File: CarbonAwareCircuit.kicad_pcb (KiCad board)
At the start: 2 copper layers, 64 x 55.5 mm, 15 parts, among them J1 USB_C_Receptacle_USB2.0_14P, J2 USB_A, Q1 AO3401A, SW1 SW_Push, SW2 SW_Push, U1 LD1117V, U2 ESP32-C3-WROOM-02

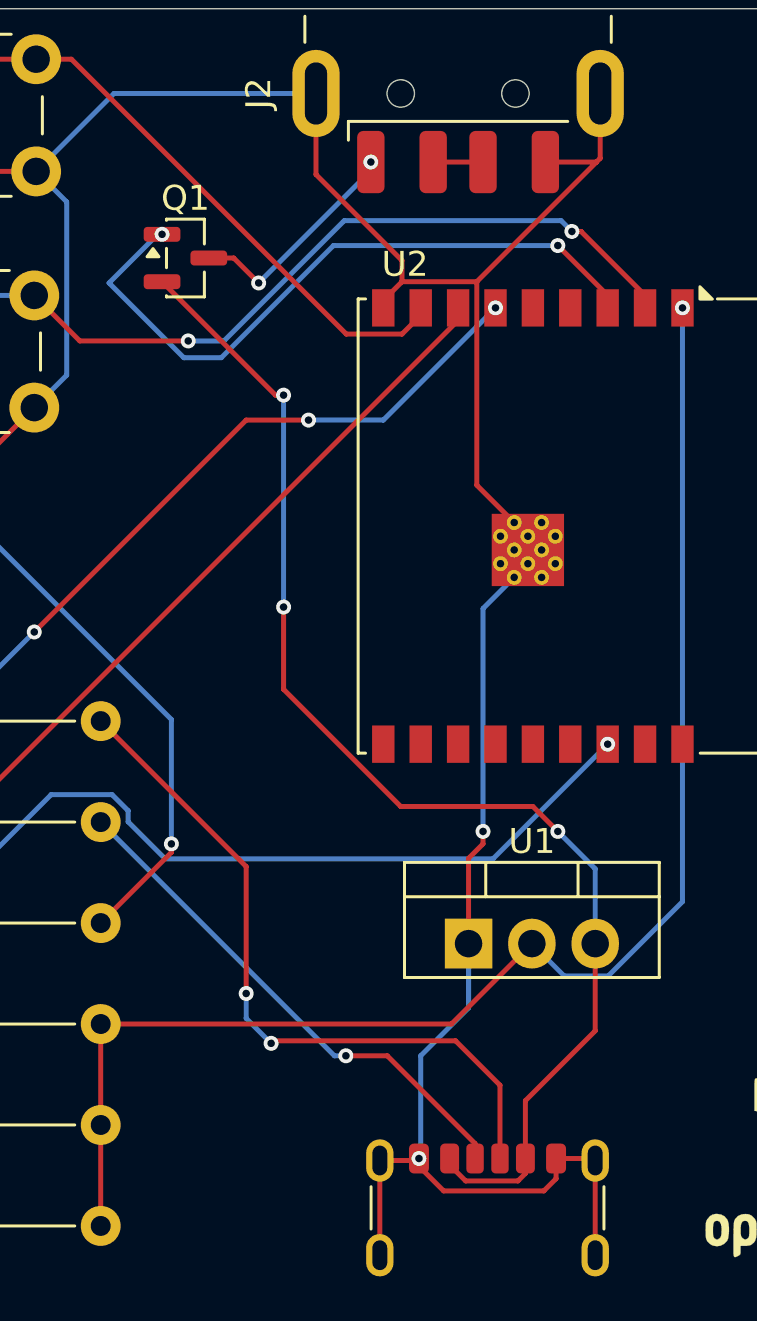
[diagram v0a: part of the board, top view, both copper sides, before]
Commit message: made traces THICK
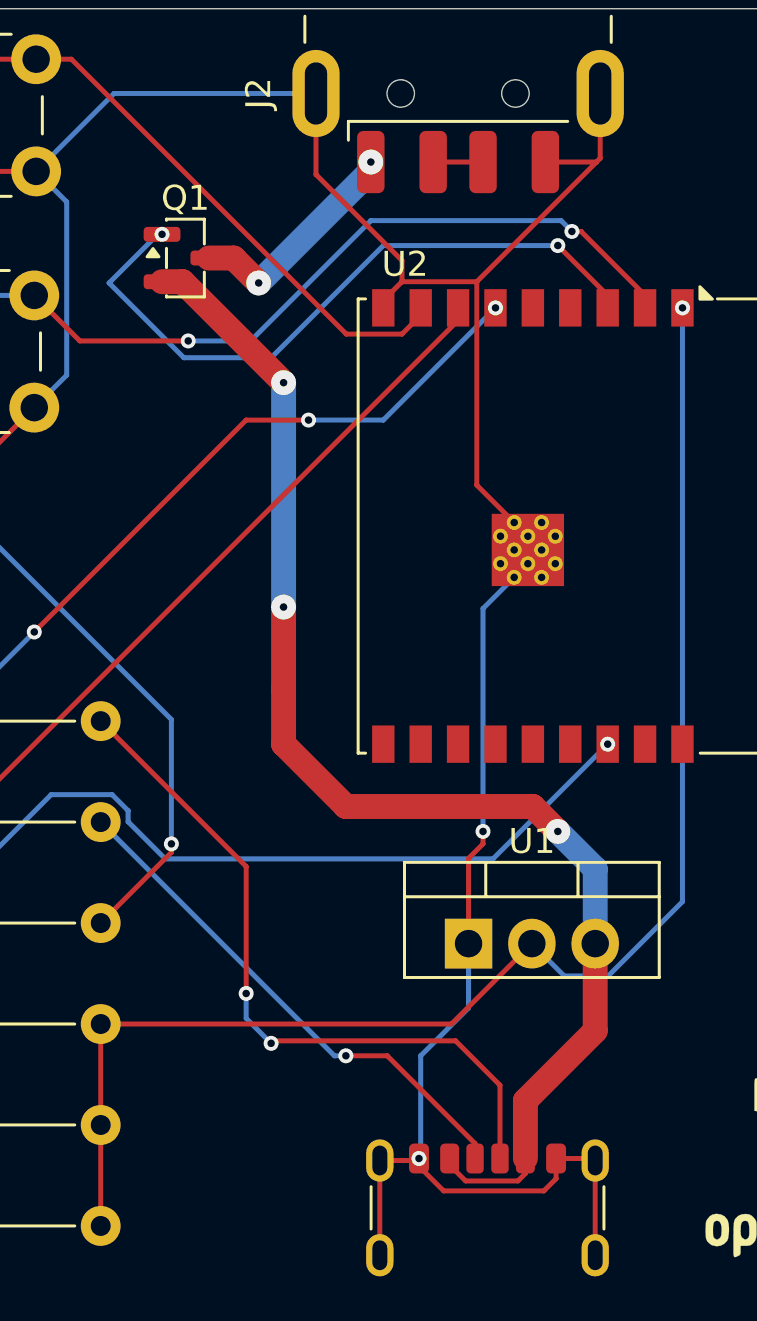
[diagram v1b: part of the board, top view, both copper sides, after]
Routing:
- net Net-(Q1-S): track 51.1 -> 52.7 mm
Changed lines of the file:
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@@
 	)
 	(gr_text "Designed by Abhiram Vadali - CompSci Team C6\n"
-		(at 197.5 97.5 180)
+		(at 255 134 325)
 		(layer "B.SilkS")
 		(effects
 			(font
-				(size 1.5 1.5)
-				(thickness 0.3)
+				(size 2 2)
+				(thickness 0.375)
 				(bold yes)
 			)
@@
 	)
 	(segment
+		(start 221.174265 101.325735)
+		(end 218.674265 101.325735)
+		(width 0.2)
+		(layer "B.Cu")
+		(net "Net-(U2-EN)")
+	)
+	(segment
 		(start 234.065687 96.934313)
 		(end 233.631374 96.5)
@@
 	)
 	(segment
-		(start 220.108579 101.325735)
-		(end 218.674265 101.325735)
+		(start 233.631374 96.5)
+		(end 226 96.5)
 		(width 0.2)
 		(layer "B.Cu")
@@
 	)
 	(segment
-		(start 224.934314 96.5)
-		(end 220.108579 101.325735)
-		(width 0.2)
-		(layer "B.Cu")
-		(net "Net-(U2-EN)")
-	)
-	(segment
-		(start 233.631374 96.5)
-		(end 224.934314 96.5)
+		(start 226 96.5)
+		(end 221.174265 101.325735)
 		(width 0.2)
 		(layer "B.Cu")
@@
 		(start 220.5 98)
 		(end 221.5 99)
-		(width 0.2)
+		(width 1)
 		(layer "F.Cu")
 		(net "Net-(J2-VBUS)")
@@
 		(start 219.5 98)
 		(end 220.5 98)
-		(width 0.2)
+		(width 1)
 		(layer "F.Cu")
 		(net "Net-(J2-VBUS)")
@@
 	(via
 		(at 226 94.15)
-		(size 0.6)
+		(size 1)
 		(drill 0.3)
 		(layers "F.Cu" "B.Cu")
@@
 	(via
 		(at 221.5 99)
-		(size 0.6)
+		(size 1)
 		(drill 0.3)
 		(layers "F.Cu" "B.Cu")
@@
 		(start 221.5 99)
 		(end 226 94.5)
-		(width 0.2)
+		(width 1)
 		(layer "B.Cu")
 		(net "Net-(J2-VBUS)")
@@
 	)
 	(segment
+		(start 233.5 97.5)
+		(end 226.5 97.5)
+		(width 0.2)
+		(layer "B.Cu")
+		(net "Net-(Q1-G)")
+	)
+	(segment
+		(start 215.5 99)
+		(end 217.45 97.05)
+		(width 0.2)
+		(layer "B.Cu")
+		(net "Net-(Q1-G)")
+	)
+	(segment
+		(start 222 102)
+		(end 218.5 102)
+		(width 0.2)
+		(layer "B.Cu")
+		(net "Net-(Q1-G)")
+	)
+	(segment
+		(start 226.5 97.5)
+		(end 222 102)
+		(width 0.2)
+		(layer "B.Cu")
+		(net "Net-(Q1-G)")
+	)
+	(segment
+		(start 217.45 97.05)
+		(end 217.625 97.05)
+		(width 0.2)
+		(layer "B.Cu")
+		(net "Net-(Q1-G)")
+	)
+	(segment
 		(start 218.5 102)
 		(end 215.5 99)
@@
 		(net "Net-(Q1-G)")
 	)
-	(segment
-		(start 220 102)
-		(end 218.5 102)
-		(width 0.2)
-		(layer "B.Cu")
-		(net "Net-(Q1-G)")
-	)
-	(segment
-		(start 224.5 97.5)
-		(end 220 102)
-		(width 0.2)
-		(layer "B.Cu")
-		(net "Net-(Q1-G)")
-	)
-	(segment
-		(start 215.5 99)
-		(end 217.45 97.05)
-		(width 0.2)
-		(layer "B.Cu")
-		(net "Net-(Q1-G)")
-	)
-	(segment
-		(start 233.5 97.5)
-		(end 224.5 97.5)
-		(width 0.2)
-		(layer "B.Cu")
-		(net "Net-(Q1-G)")
-	)
-	(segment
-		(start 217.45 97.05)
-		(end 217.625 97.05)
-		(width 0.2)
-		(layer "B.Cu")
-		(net "Net-(Q1-G)")
-	)
 	(via
 		(at 235.5 117.5)
@@
 	)
 	(segment
+		(start 232.5 120)
+		(end 225 120)
+		(width 1)
+		(layer "F.Cu")
+		(net "Net-(Q1-S)")
+	)
+	(segment
+		(start 235 129)
+		(end 232.2 131.8)
+		(width 1)
+		(layer "F.Cu")
+		(net "Net-(Q1-S)")
+	)
+	(segment
+		(start 229.803398 135.02)
+		(end 231.9 135.02)
+		(width 0.2)
+		(layer "F.Cu")
+		(net "Net-(Q1-S)")
+	)
+	(segment
+		(start 218.45 98.95)
+		(end 217.625 98.95)
+		(width 1)
+		(layer "F.Cu")
+		(net "Net-(Q1-S)")
+	)
+	(segment
+		(start 222.5 103)
+		(end 218.45 98.95)
+		(width 1)
+		(layer "F.Cu")
+		(net "Net-(Q1-S)")
+	)
+	(segment
+		(start 235 125.5)
+		(end 235 129)
+		(width 1)
+		(layer "F.Cu")
+		(net "Net-(Q1-S)")
+	)
+	(segment
 		(start 233.5 121)
 		(end 232.5 120)
-		(width 0.2)
-		(layer "F.Cu")
-		(net "Net-(Q1-S)")
-	)
-	(segment
-		(start 222.175 103.5)
-		(end 222.5 103.5)
-		(width 0.2)
-		(layer "F.Cu")
-		(net "Net-(Q1-S)")
-	)
-	(segment
-		(start 229.803398 135.02)
-		(end 231.9 135.02)
-		(width 0.2)
-		(layer "F.Cu")
-		(net "Net-(Q1-S)")
-	)
-	(segment
-		(start 235 129)
-		(end 232.2 131.8)
-		(width 0.2)
+		(width 1)
 		(layer "F.Cu")
 		(net "Net-(Q1-S)")
@@
 		(start 222.5 115.3)
 		(end 222.5 112)
-		(width 0.2)
-		(layer "F.Cu")
-		(net "Net-(Q1-S)")
-	)
-	(segment
-		(start 235 129)
-		(end 235 125.5)
-		(width 0.2)
-		(layer "F.Cu")
-		(net "Net-(Q1-S)")
-	)
-	(segment
-		(start 227.2 120)
-		(end 222.5 115.3)
-		(width 0.2)
+		(width 1)
 		(layer "F.Cu")
 		(net "Net-(Q1-S)")
@@
 	)
 	(segment
-		(start 232.5 120)
-		(end 227.2 120)
-		(width 0.2)
-		(layer "F.Cu")
-		(net "Net-(Q1-S)")
-	)
-	(segment
 		(start 232.2 134.72)
 		(end 232.2 134.12)
@@
 	)
 	(segment
-		(start 217.625 98.95)
-		(end 222.175 103.5)
-		(width 0.2)
-		(layer "F.Cu")
-		(net "Net-(Q1-S)")
-	)
-	(segment
 		(start 232.2 131.8)
 		(end 232.2 134.12)
-		(width 0.2)
+		(width 1)
+		(layer "F.Cu")
+		(net "Net-(Q1-S)")
+	)
+	(segment
+		(start 222.5 117.5)
+		(end 222.5 115.3)
+		(width 1)
+		(layer "F.Cu")
+		(net "Net-(Q1-S)")
+	)
+	(segment
+		(start 225 120)
+		(end 222.5 117.5)
+		(width 1)
 		(layer "F.Cu")
 		(net "Net-(Q1-S)")
@@
 	(via
 		(at 222.5 112)
-		(size 0.6)
+		(size 1)
+		(drill 0.3)
+		(layers "F.Cu" "B.Cu")
+		(net "Net-(Q1-S)")
+	)
+	(via
+		(at 222.5 103)
+		(size 1)
 		(drill 0.3)
 		(layers "F.Cu" "B.Cu")
@@
 	(via
 		(at 233.5 121)
-		(size 0.6)
-		(drill 0.3)
-		(layers "F.Cu" "B.Cu")
-		(net "Net-(Q1-S)")
-	)
-	(via
-		(at 222.5 103.5)
-		(size 0.6)
-		(drill 0.3)
-		(layers "F.Cu" "B.Cu")
-		(net "Net-(Q1-S)")
-	)
-	(segment
-		(start 222.5 112)
-		(end 222.5 103.5)
-		(width 0.2)
+		(size 1)
+		(drill 0.3)
+		(layers "F.Cu" "B.Cu")
+		(net "Net-(Q1-S)")
+	)
+	(segment
+		(start 235 122.5)
+		(end 235 125.5)
+		(width 1)
 		(layer "B.Cu")
 		(net "Net-(Q1-S)")
@@
 		(start 235 122.5)
 		(end 233.5 121)
-		(width 0.2)
-		(layer "B.Cu")
-		(net "Net-(Q1-S)")
-	)
-	(segment
-		(start 235 125.5)
-		(end 235 122.5)
-		(width 0.2)
-		(layer "B.Cu")
-		(net "Net-(Q1-S)")
+		(width 1)
+		(layer "B.Cu")
+		(net "Net-(Q1-S)")
+	)
+	(segment
+		(start 222.5 112)
+		(end 222.5 103)
+		(width 1)
+		(layer "B.Cu")
+		(net "Net-(Q1-S)")
